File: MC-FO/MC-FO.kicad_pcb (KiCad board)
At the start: 4 copper layers, 160 x 100 mm, 93 parts, among them U101 74ACT08SCX, U102 IFE98, U121 74ACT08SCX, U122 IFE98, U141 IFD97, U142 TLV3501AID, U143 74LVC1G32SE-7, U161 IFD97, U163 74LVC1G32SE-7, U181 TPS3703A5330DSER, U182 TPS3703A5500DSER, U183 74ACT08SCX, U184 74LVC1G07QDCKTQ1, U2 R-78E3.3-0.5, U27 74ACT08SCX, U28 IFE98, U3 R-78E5.0-0.5, U41 74ACT08SCX, U42 IFE98, U61 74ACT08SCX, U62 IFE98, U81 74ACT08SCX, U82 IFE98

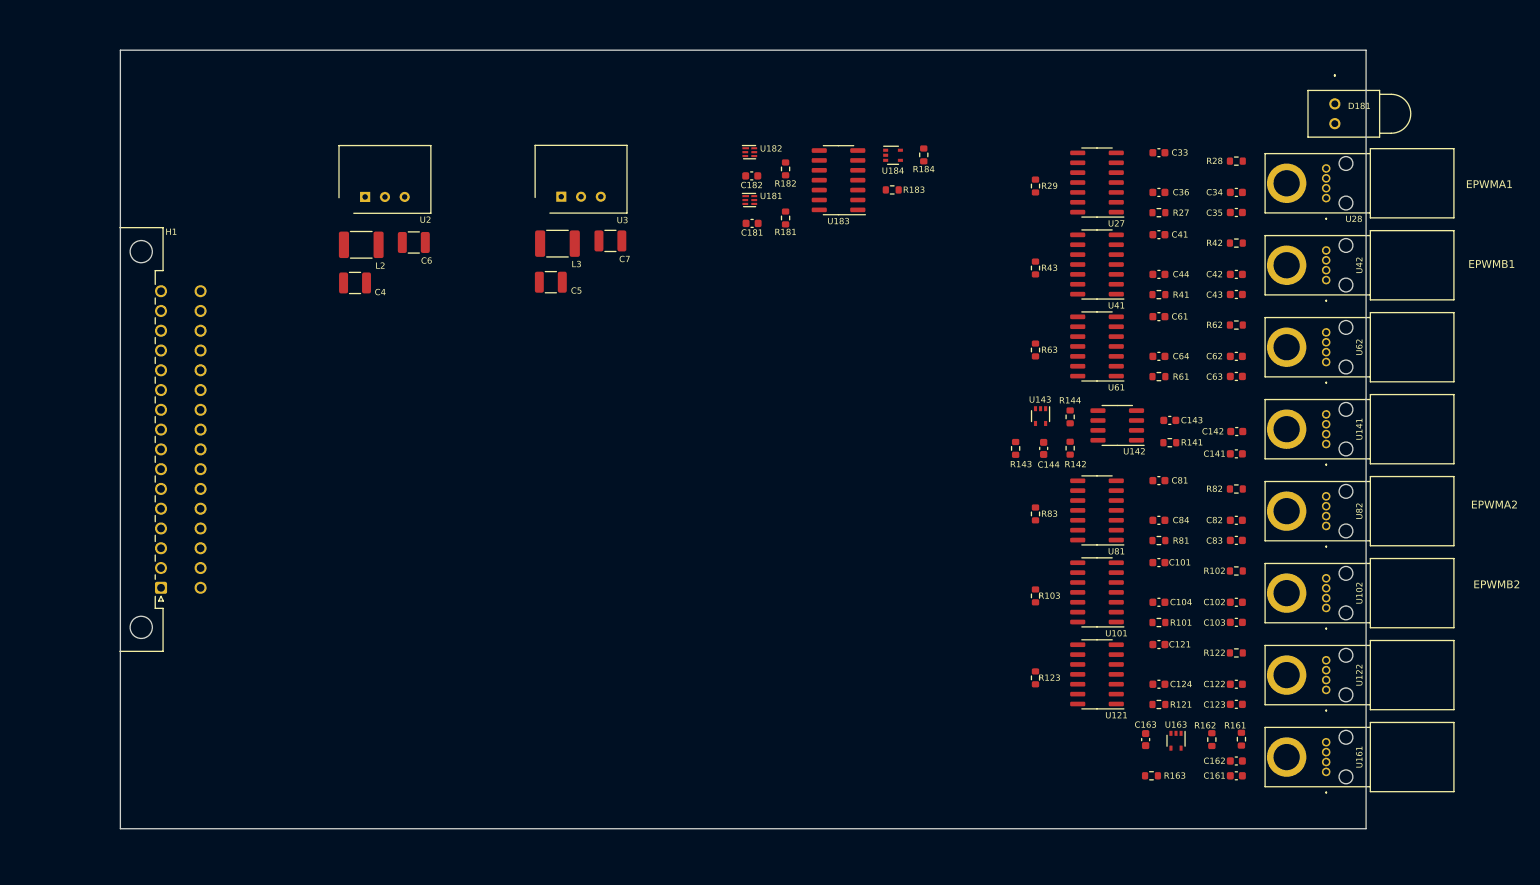
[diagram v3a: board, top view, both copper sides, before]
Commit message: Routed FO schematic
All FO circuits routed except LED and Detector circuits.
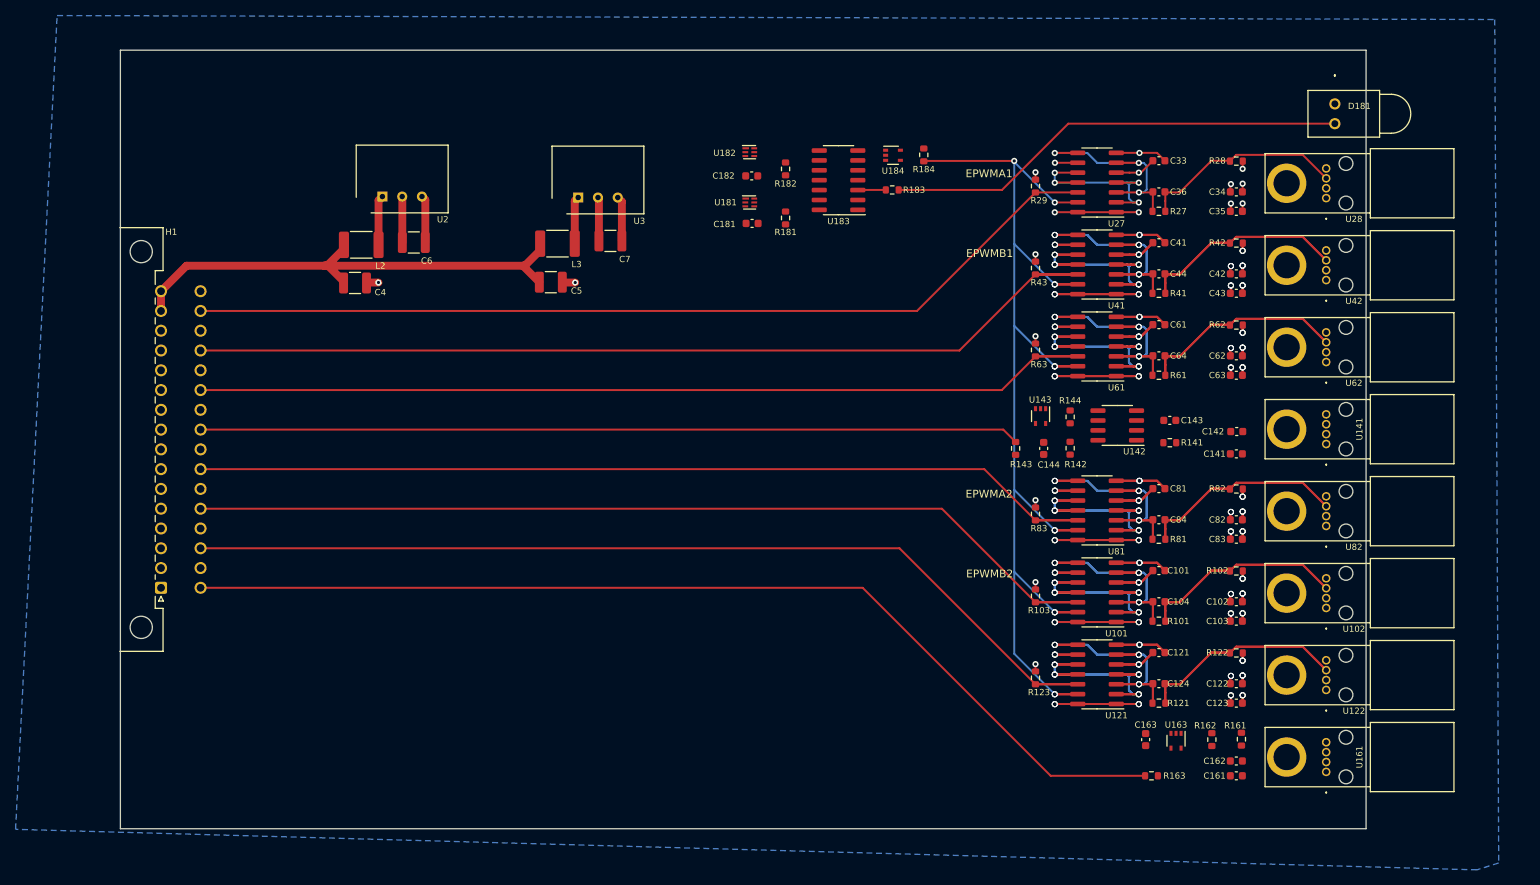
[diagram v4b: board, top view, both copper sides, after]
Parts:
- moved U2 2.22 mm to (120.0, 69.6)
- moved U3 2.17 mm to (145.2, 69.7)
- moved C101 1.03 mm to (219.8, 117.6)
- moved C121 1.03 mm to (219.8, 128.2)
- moved C33 1.03 mm to (219.8, 65.0)
- moved C41 1.03 mm to (219.8, 75.5)
- moved C61 1.03 mm to (219.8, 86.1)
- moved C81 1.03 mm to (219.8, 107.1)
- moved U181 0.31 mm to (167.2, 70.4)
- moved R101 0.17 mm to (219.8, 124.1)
- moved R27 0.17 mm to (219.8, 71.5)
- moved R41 0.17 mm to (219.8, 82.0)
- moved R61 0.17 mm to (219.8, 92.6)
- moved R81 0.17 mm to (219.8, 113.6)
- moved R121 0.17 mm to (219.8, 134.7)
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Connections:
- H1 pad 15: GND -> 24V
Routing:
- net /Detector1/5V: track 0.00 -> 253.1 mm, vias 0 -> 77
- net /Emitter1/RESET_FO: track 0.00 -> 150.9 mm, vias 0 -> 12
- net STATUS2: track 0.00 -> 131.3 mm
- net EPWM1B: track 0.00 -> 127.6 mm
- net RESET2: track 0.00 -> 125.3 mm
- net EPWM2B: track 0.00 -> 123.1 mm
- net GND: track 0.00 -> 121.5 mm, vias 0 -> 41
- net EPWM2A: track 0.00 -> 120.8 mm
- net RESET1: track 0.00 -> 119.9 mm
- net EPWM1A: track 0.00 -> 119.0 mm
- net STATUS1: track 0.00 -> 105.3 mm
- net 24V: track 0.00 -> 64.8 mm
- net Net-(C64-Pad1): track 0.00 -> 61.7 mm, vias 0 -> 6
- net Net-(C44-Pad1): track 0.00 -> 61.7 mm, vias 0 -> 6
- net Net-(C84-Pad1): track 0.00 -> 61.7 mm, vias 0 -> 6
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- added copper zone on B.Cu, net /Detector1/5V
- added copper zone on GND1.Cu, net GND
- added copper zone on GND2.Cu, net GND

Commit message: Changed V-monitor circuit, V-reg circuit, finished detectors
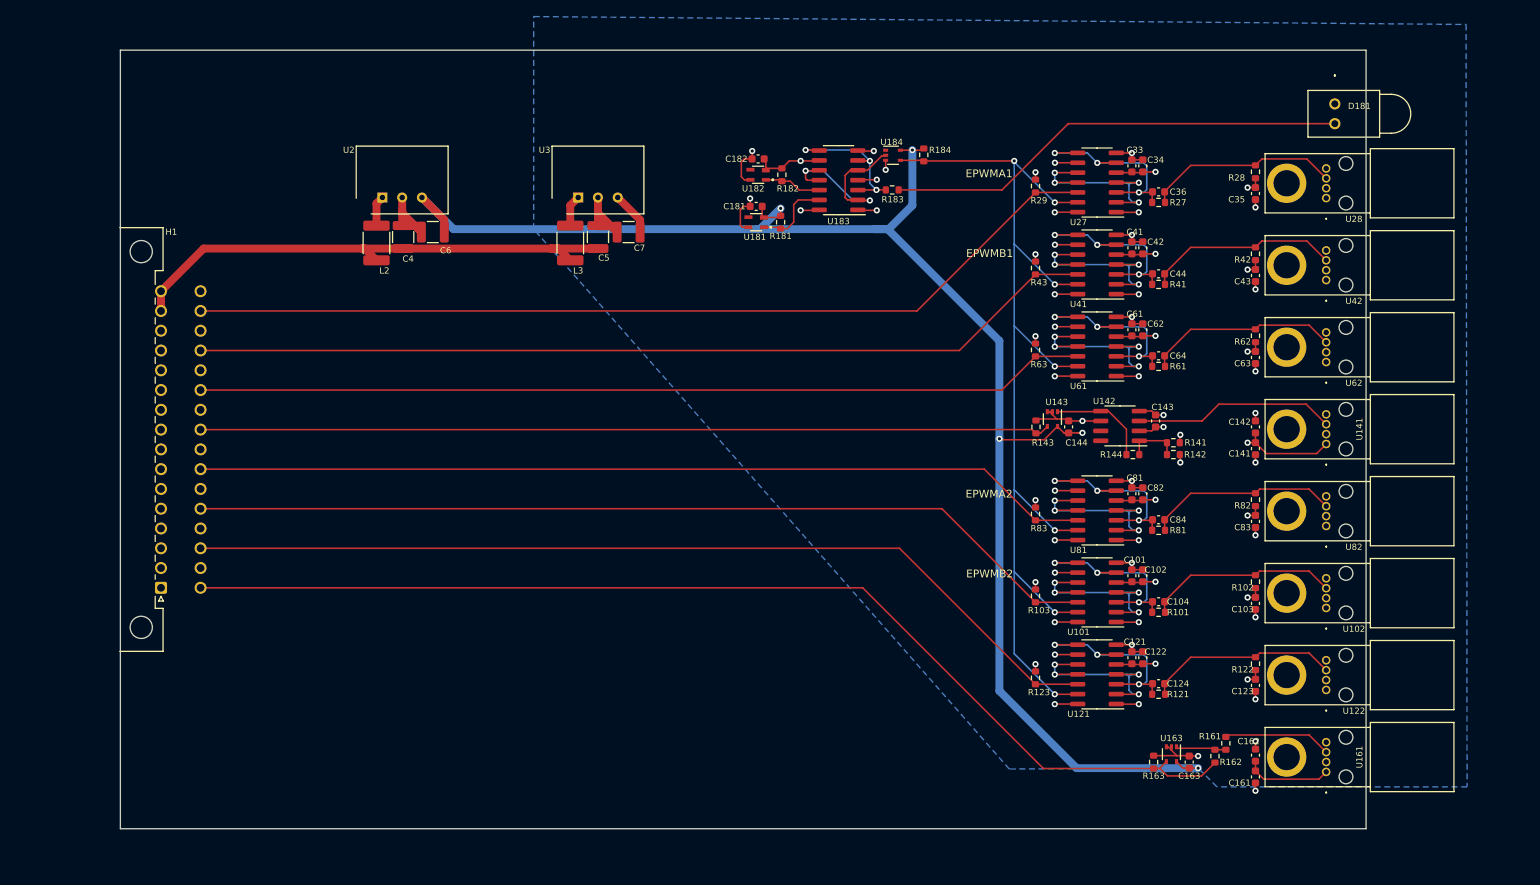
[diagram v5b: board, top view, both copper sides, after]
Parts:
- U181: value TPS3703A5330DSER -> BU4831F-TR; footprint Package_SON:WSON-6_1.5x1.5mm_P0.5mm -> BU4847F-TR:SOT130P210X105-4N
- U182: value TPS3703A5500DSER -> BU4847F-TR; footprint Package_SON:WSON-6_1.5x1.5mm_P0.5mm -> BU4847F-TR:SOT130P210X105-4N
- moved R142 13.3 mm to (221.6, 102.7), turned to 180 degrees
- moved C122 12.5 mm to (217.7, 128.8), turned to 90 degrees
- moved C102 12.5 mm to (217.7, 118.3), turned to 90 degrees
- moved C34 12.5 mm to (217.7, 65.7), turned to 90 degrees
- moved C42 12.5 mm to (217.7, 76.2), turned to 90 degrees
- moved C62 12.5 mm to (217.7, 86.7), turned to 90 degrees
- moved C82 12.5 mm to (217.7, 107.8), turned to 90 degrees
- moved R144 9.40 mm to (216.4, 102.7), turned to 180 degrees
- moved C4 8.54 mm to (122.7, 74.8), turned to 90 degrees
- moved C5 8.38 mm to (147.7, 74.8), turned to 90 degrees
- moved C163 6.30 mm to (223.6, 142.2)
- moved C144 4.23 mm to (208.2, 99.2), turned to 90 degrees
- moved R143 3.80 mm to (204.0, 99.2), turned to 90 degrees
- moved C101 3.53 mm to (216.3, 118.3), turned to 90 degrees
- moved C33 3.53 mm to (216.3, 65.7), turned to 90 degrees
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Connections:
- C181 pad 1: Net-(C181-Pad1) -> VCC
- C182 pad 1: Net-(C182-Pad1) -> /Detector1/5V
- R182 pad 1: VCC -> /Detector1/5V
- U181 pad 1: VCC -> Net-(R181-Pad2)
- U181 pad 3: Net-(C181-Pad1) -> Net-(U181-Pad3)
- U181 pad 4: Net-(R181-Pad2) -> GND
- U182 pad 1: /Detector1/5V -> Net-(R182-Pad2)
- U182 pad 3: Net-(C182-Pad1) -> Net-(U182-Pad3)
- U182 pad 4: Net-(R182-Pad2) -> GND
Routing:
- net VCC: track 6.08 -> 202.4 mm, vias 0 -> 5
- net /Detector1/5V: track 253.1 -> 147.6 mm, vias 77 -> 37
- net Net-(C64-Pad1): track 61.7 -> 29.1 mm, vias 6 -> 3
- net Net-(C44-Pad1): track 61.7 -> 29.1 mm, vias 6 -> 3
- net Net-(C124-Pad1): track 61.7 -> 29.1 mm, vias 6 -> 3
- net Net-(C84-Pad1): track 61.7 -> 29.1 mm, vias 6 -> 3
- net Net-(C104-Pad1): track 61.7 -> 29.1 mm, vias 6 -> 3
- net Net-(C124-Pad2): track 53.2 -> 24.8 mm
- net Net-(C84-Pad2): track 53.2 -> 24.8 mm
- net Net-(C104-Pad2): track 53.2 -> 24.8 mm
- net Net-(C64-Pad2): track 53.2 -> 24.8 mm
- net Net-(U183-Pad10): track 0.00 -> 28.3 mm, vias 0 -> 2
- net Net-(C44-Pad2): track 53.2 -> 25.0 mm
- net Net-(U81-Pad10): track 55.5 -> 27.8 mm, vias 8 -> 4
- net Net-(U101-Pad10): track 55.5 -> 27.8 mm, vias 8 -> 4
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
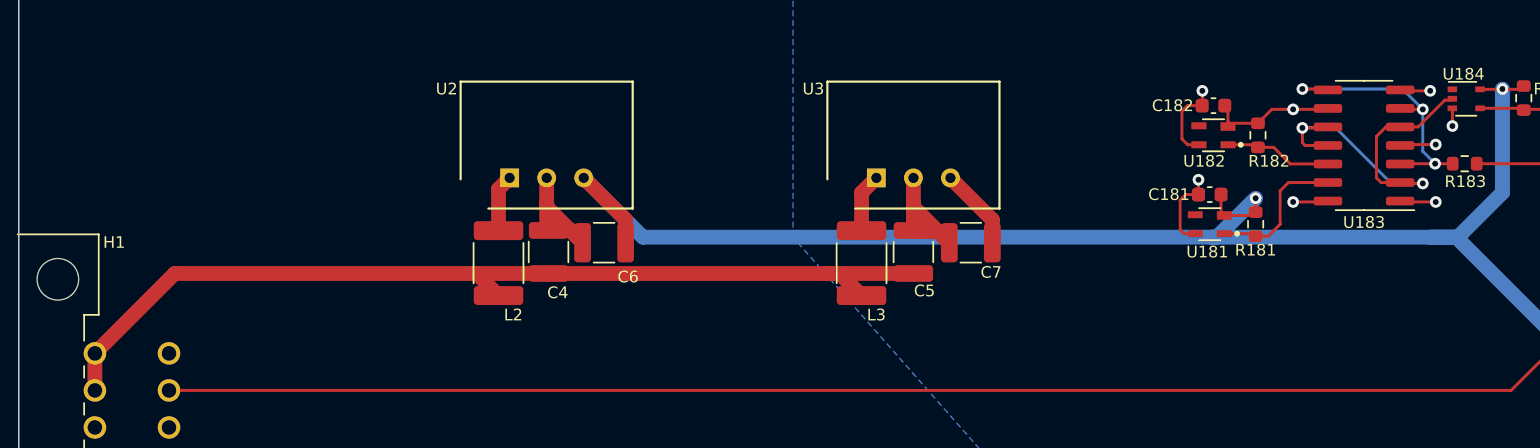
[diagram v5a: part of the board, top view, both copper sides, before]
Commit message: 24V line and LED ckrt fix
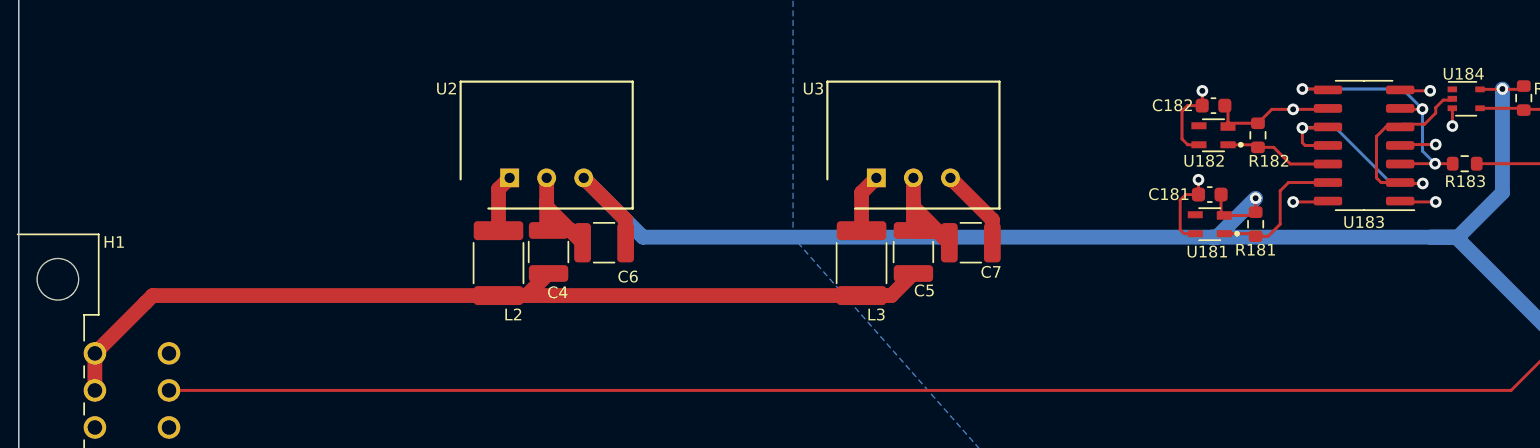
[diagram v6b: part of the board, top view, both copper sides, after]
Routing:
- net 24V: track 66.5 -> 63.1 mm
